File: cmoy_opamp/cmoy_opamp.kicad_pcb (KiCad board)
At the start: 2 copper layers, 79.2 x 67.6 mm, 33 parts, among them J1 AudioJack3, J2 AudioJack3, SW1 SPST, U1 MC33178, U2 LMH6642, U3 LMH6642, U4 LMH6642

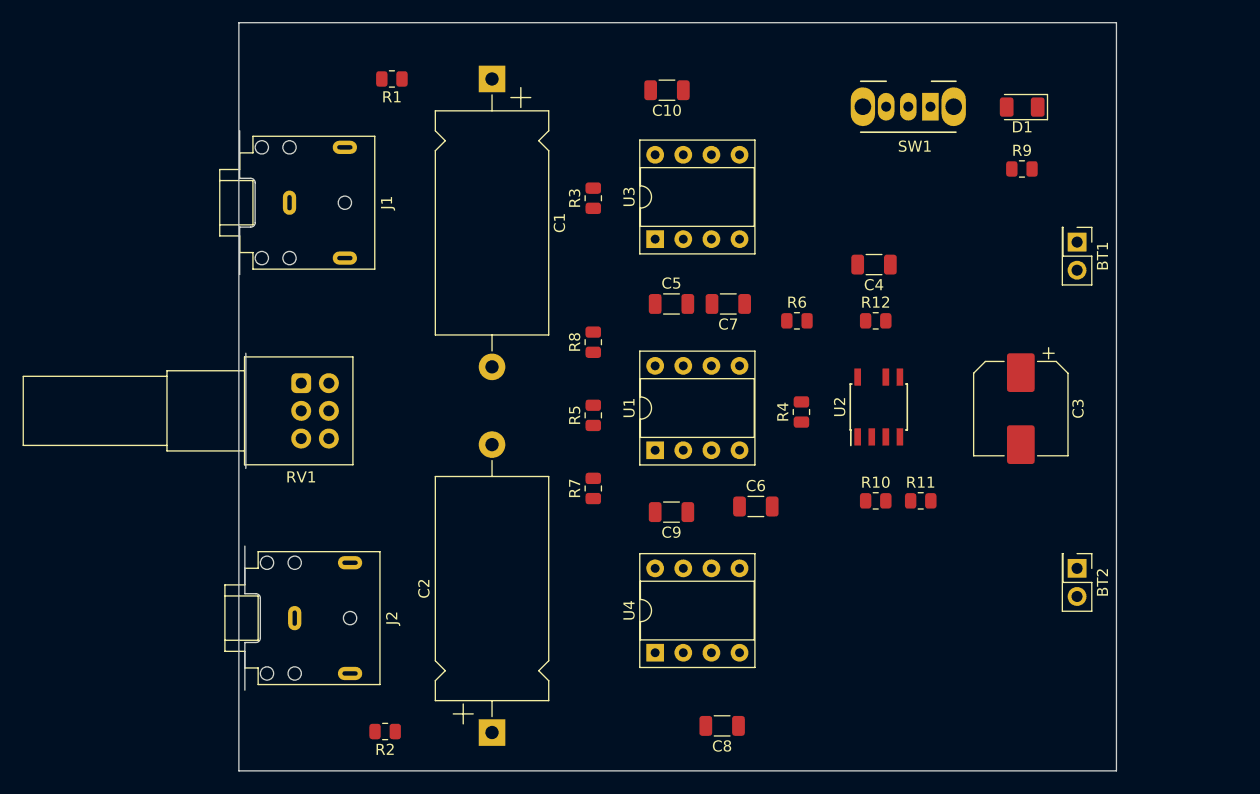
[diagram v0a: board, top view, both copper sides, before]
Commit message: dual footprint, THT and SMD, first layouting
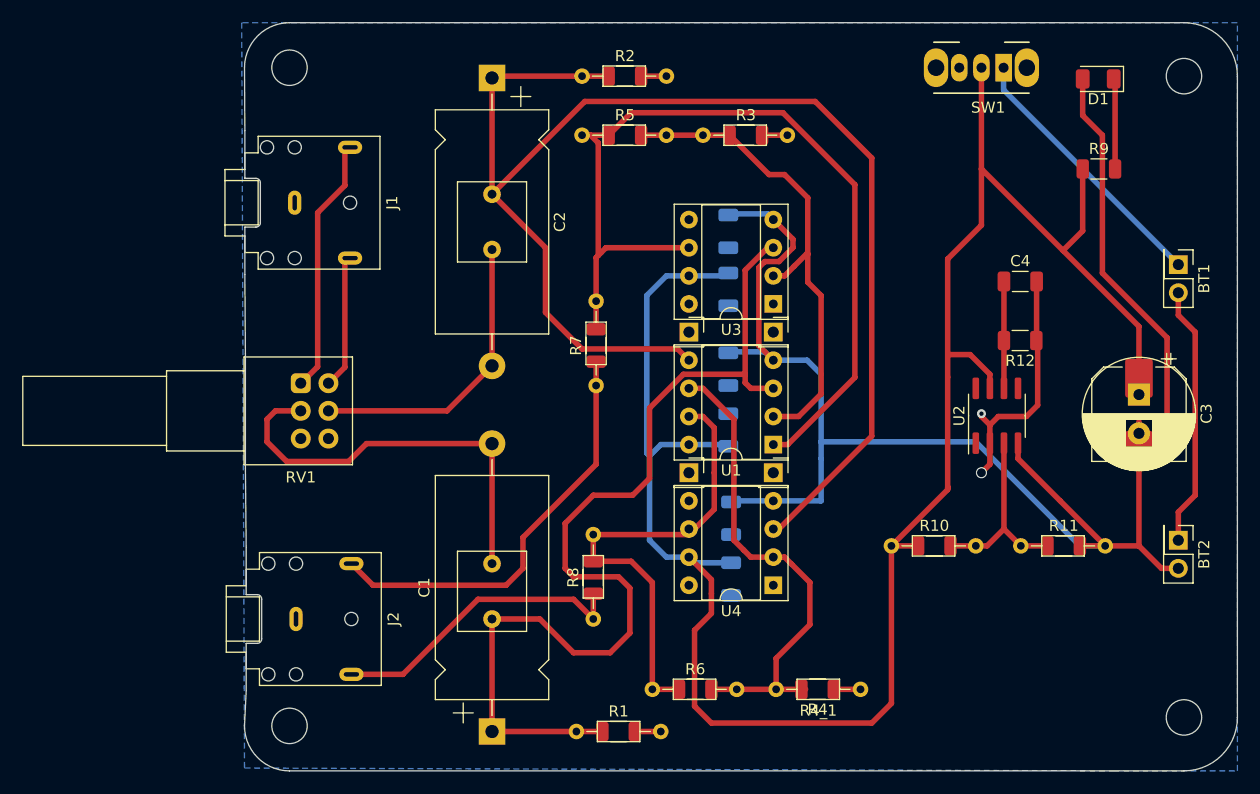
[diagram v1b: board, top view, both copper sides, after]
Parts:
- added C1_1: 0,1µF, Capacitor_THT:C_Rect_L7.0mm_W6.0mm_P5.00mm, F.Cu at (171.7, 92.0)
- added C2_1: 0,1µF, Capacitor_THT:C_Rect_L7.0mm_W6.0mm_P5.00mm, F.Cu at (171.7, 63.7)
- added C3_1: 220µF, Capacitor_THT:CP_Radial_D10.0mm_P3.50mm, F.Cu at (230.1, 76.8)
- added R10_1: 220k, Resistor_THT:R_Axial_DIN0204_L3.6mm_D1.6mm_P7.62mm_Horizontal, F.Cu at (207.8, 90.4)
- added R11_1: 220k, Resistor_THT:R_Axial_DIN0204_L3.6mm_D1.6mm_P7.62mm_Horizontal, F.Cu at (219.5, 90.4)
- added R1_1: 100k, Resistor_THT:R_Axial_DIN0204_L3.6mm_D1.6mm_P7.62mm_Horizontal, F.Cu at (179.3, 107.2)
- added R2_1: 100k, Resistor_THT:R_Axial_DIN0204_L3.6mm_D1.6mm_P7.62mm_Horizontal, F.Cu at (179.8, 48.0)
- added R3_1: 1k, Resistor_THT:R_Axial_DIN0204_L3.6mm_D1.6mm_P7.62mm_Horizontal, F.Cu at (190.8, 53.3)
- added R4_1: 1k, Resistor_THT:R_Axial_DIN0204_L3.6mm_D1.6mm_P7.62mm_Horizontal, F.Cu at (205.0, 103.4)
- added R5_1: 10k, Resistor_THT:R_Axial_DIN0204_L3.6mm_D1.6mm_P7.62mm_Horizontal, F.Cu at (179.8, 53.3)
- added R6_1: 10k, Resistor_THT:R_Axial_DIN0204_L3.6mm_D1.6mm_P7.62mm_Horizontal, F.Cu at (186.2, 103.4)
- added R7_1: 38, Resistor_THT:R_Axial_DIN0204_L3.6mm_D1.6mm_P7.62mm_Horizontal, F.Cu at (181.1, 75.9)
- added R8_1: 38, Resistor_THT:R_Axial_DIN0204_L3.6mm_D1.6mm_P7.62mm_Horizontal, F.Cu at (180.8, 97.0)
- added REF**: MountingHole_3.2mm_M3_ISO7380, MountingHole:MountingHole_3.2mm_M3_ISO7380, F.Cu at (153.4, 47.2)
- added REF**: MountingHole_3.2mm_M3_ISO7380, MountingHole:MountingHole_3.2mm_M3_ISO7380, F.Cu at (234.2, 105.9)
- added REF**: MountingHole_3.2mm_M3_ISO7380, MountingHole:MountingHole_3.2mm_M3_ISO7380, F.Cu at (234.2, 48.0)
- added REF**: MountingHole_3.2mm_M3_ISO7380, MountingHole:MountingHole_3.2mm_M3_ISO7380, F.Cu at (153.4, 106.7)
- added TP1: TestPoint, Connector_PinSocket_2.54mm:PinSocket_1x01_P2.54mm_Vertical, F.Cu at (189.5, 71.1)
- added TP2: TestPoint, Connector_PinSocket_2.54mm:PinSocket_1x01_P2.54mm_Vertical, F.Cu at (197.1, 71.1)
- added TP3: TestPoint, Connector_PinSocket_2.54mm:PinSocket_1x01_P2.54mm_Vertical, F.Cu at (189.5, 83.8)
- added TP4: TestPoint, Connector_PinSocket_2.54mm:PinSocket_1x01_P2.54mm_Vertical, F.Cu at (197.1, 83.8)
- C10, C5, C6, C7, C8, C9: moved to B.Cu
- R1, R10, R11, R12, R2, R3, R4, R5, R6, R7, R8, R9: footprint Resistor_SMD:R_0805_2012Metric -> Resistor_SMD:R_1206_3216Metric
- U2: footprint Package_SO:SOIC-8-N7_3.9x4.9mm_P1.27mm -> Package_SO:SOIC-8_3.9x4.9mm_P1.27mm
- moved R2 63.0 mm to (183.7, 48.0), turned to 0 degrees
- moved R1 62.4 mm to (183.1, 107.2), turned to 0 degrees
- moved C2 59.1 mm to (171.7, 48.2), turned to -90 degrees
- moved C1 58.9 mm to (171.7, 107.2), turned to 90 degrees
- moved R6 34.5 mm to (190.1, 103.4)
- moved R5 25.5 mm to (183.7, 53.3), turned to 0 degrees
- moved R4 25.1 mm to (201.1, 103.4), turned to 180 degrees
- moved R8 21.2 mm to (180.8, 93.3)
- moved C10 18.8 mm to (193.0, 67.3), turned to -90 degrees
- moved C8 18.8 mm to (193.3, 87.9), turned to -90 degrees
- moved R3 14.9 mm to (194.6, 53.3), turned to 0 degrees
- moved R11 13.5 mm to (223.3, 90.4)
- moved C4 13.3 mm to (219.4, 66.5), turned to 0 degrees
- moved R12 13.2 mm to (219.4, 71.9), turned to 180 degrees
- moved R7 12.9 mm to (181.1, 72.3)
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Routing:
- net V+: track 0.00 -> 182.3 mm
- net V-: track 0.00 -> 150.0 mm
- net /2+: track 0.00 -> 126.1 mm
- net /1+: track 0.00 -> 91.3 mm
- net /1O: track 0.00 -> 81.8 mm
- net /1-: track 0.00 -> 44.7 mm
- net /2-: track 0.00 -> 44.0 mm
- net /2O: track 0.00 -> 42.5 mm
- net Net-(J2-PadR): track 0.00 -> 38.3 mm
- net Net-(C1-Pad2): track 0.00 -> 38.0 mm
- net GND: track 0.00 -> 31.3 mm, vias 0 -> 2
- net Net-(J2-PadT): track 0.00 -> 27.7 mm
- net Net-(C2-Pad2): track 0.00 -> 26.9 mm
- net Net-(BT1-+): track 0.00 -> 24.3 mm
- net Net-(BT1--): track 0.00 -> 23.6 mm
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- added copper zone on B.Cu, net GND
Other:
- board size 79.2 x 67.6 mm -> 89.7 x 67.6 mm

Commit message: PCB Layout complete
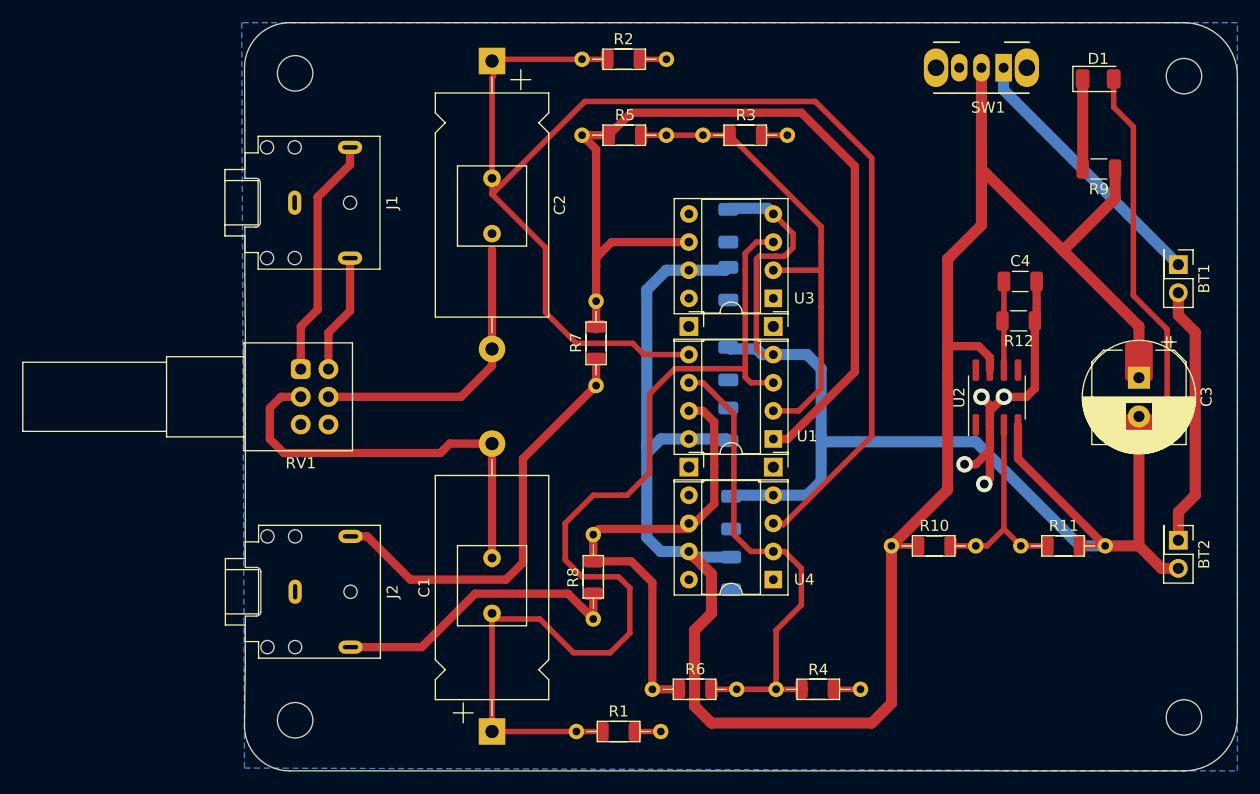
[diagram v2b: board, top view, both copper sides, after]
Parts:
- R9: value 100k -> 2k2
- moved J2 2.46 mm to (153.9, 94.6)
- moved R12 1.78 mm to (219.3, 70.1)
- moved U2 1.65 mm to (217.3, 77.0)
- moved R2 1.53 mm to (183.6, 46.5)
- moved C2 1.52 mm to (171.7, 46.6)
- moved C3 1.52 mm to (230.1, 77.0)
- moved C3_1 1.52 mm to (230.1, 75.2)
- moved R2_1 1.52 mm to (179.8, 46.5)
- moved C2_1 1.44 mm to (171.7, 62.2)
- moved RV1 1.27 mm to (154.4, 74.5)
- moved REF** 0.72 mm to (153.9, 106.2)
- moved REF** 0.72 mm to (153.9, 47.8)
- moved C1_1 0.51 mm to (171.7, 91.5)
- moved C6 0.51 mm to (193.0, 74.0)
- moved C8 0.51 mm to (193.3, 87.4)
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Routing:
- net GND: track 31.3 -> 36.1 mm, vias 2 -> 4
- net V+: track 182.3 -> 184.5 mm
- net /1O: track 81.8 -> 83.8 mm
- net Net-(C4-Pad1): track 9.65 -> 8.00 mm
- net Net-(U2-+): track 17.8 -> 19.4 mm
- net Net-(J1-PadT): track 11.9 -> 10.8 mm
- net Net-(J1-PadR): track 22.9 -> 21.9 mm
- net /1-: track 44.7 -> 43.8 mm
- net V-: track 150.0 -> 151.0 mm
- net /1+: track 91.3 -> 91.9 mm
- net Net-(J2-PadT): track 27.7 -> 27.1 mm
- net /2+: track 126.1 -> 125.6 mm
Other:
- outline, holes or cut-outs redrawn

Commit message: PCB art added
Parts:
- added G***: LOGO, pcb_art, F.Cu at (193.0, 78.2)
- added R12_1: 1k, Resistor_THT:R_Axial_DIN0204_L3.6mm_D1.6mm_P7.62mm_Horizontal, F.Cu at (223.0, 70.1)
- added REF**: OSHW-Logo2_14.6x12mm_Copper, Symbol:OSHW-Logo2_14.6x12mm_Copper, B.Cu at (222.8, 99.6)
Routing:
- net Net-(C4-Pad1): track 8.00 -> 10.4 mm
- net GND: track 36.1 -> 38.3 mm
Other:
- board text added: "www.designer2k2.at 2023"

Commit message: PCB Version ready to order
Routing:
- net Net-(C2-Pad2): track 26.4 -> 27.9 mm
- net /2+: track 125.6 -> 126.3 mm
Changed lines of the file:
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@@
   (segment (start 182.241 46.482) (end 179.832 46.482) (width 0.5) (layer "F.Cu") (net 6))
   (segment (start 180.08 50.292) (end 200.887949 50.292) (width 0.5) (layer "F.Cu") (net 6))
-  (segment (start 171.866 48.006) (end 171.704 48.168) (width 0.5) (layer "F.Cu") (net 6))
+  (segment (start 178.562 50.292) (end 180.08 50.292) (width 0.5) (layer "F.Cu") (net 6))
+  (segment (start 171.704 57.23) (end 177.88 51.054) (width 0.5) (layer "F.Cu") (net 6))
   (segment (start 197.104 88.392) (end 197.866 88.392) (width 0.5) (layer "F.Cu") (net 6))
+  (segment (start 177.88 51.054) (end 177.88 50.974) (width 0.5) (layer "F.Cu") (net 6))
   (segment (start 189.484 73.152) (end 185.42 73.152) (width 0.5) (layer "F.Cu") (net 6))
   (segment (start 179.751 46.482) (end 171.785 46.482) (width 0.5) (layer "F.Cu") (net 6))
   (segment (start 205.994 80.518) (end 197.993 88.519) (width 0.5) (layer "F.Cu") (net 6))
   (segment (start 200.887949 50.292) (end 205.994 55.398051) (width 0.5) (layer "F.Cu") (net 6))
-  (segment (start 176.53 63.494) (end 176.53 69.342) (width 0.5) (layer "F.Cu") (net 6))
   (segment (start 176.53 69.342) (end 179.324 72.136) (width 0.5) (layer "F.Cu") (net 6))
+  (segment (start 176.53 62.056) (end 176.53 63.754) (width 0.5) (layer "F.Cu") (net 6))
   (segment (start 197.866 88.392) (end 197.993 88.519) (width 0.5) (layer "F.Cu") (net 6))
-  (segment (start 171.704 48.168) (end 171.704 58.668) (width 0.5) (layer "F.Cu") (net 6))
   (segment (start 179.324 72.136) (end 184.404 72.136) (width 0.5) (layer "F.Cu") (net 6))
   (segment (start 205.994 55.398051) (end 205.994 80.518) (width 0.5) (layer "F.Cu") (net 6))
-  (segment (start 171.704 58.668) (end 176.53 63.494) (width 0.5) (layer "F.Cu") (net 6))
-  (segment (start 171.704 58.668) (end 180.08 50.292) (width 0.5) (layer "F.Cu") (net 6))
+  (segment (start 171.704 57.23) (end 171.704 46.644) (width 0.5) (layer "F.Cu") (net 6))
+  (segment (start 171.704 57.23) (end 176.53 62.056) (width 0.5) (layer "F.Cu") (net 6))
+  (segment (start 176.53 63.754) (end 176.53 69.342) (width 0.5) (layer "F.Cu") (net 6))
+  (segment (start 177.88 50.974) (end 178.562 50.292) (width 0.5) (layer "F.Cu") (net 6))
   (segment (start 185.42 73.152) (end 184.404 72.136) (width 0.5) (layer "F.Cu") (net 6))
+  (segment (start 156.932 76.962) (end 168.91 76.962) (width 0.75) (layer "F.Cu") (net 7))
   (segment (start 168.91 76.962) (end 171.704 74.168) (width 0.75) (layer "F.Cu") (net 7))
-  (segment (start 156.932 76.962) (end 168.91 76.962) (width 0.75) (layer "F.Cu") (net 7))
-  (segment (start 171.704 63.668) (end 171.704 74.168) (width 0.75) (layer "F.Cu") (net 7))
+  (segment (start 171.704 74.168) (end 171.704 62.23) (width 0.75) (layer "F.Cu") (net 7))
   (segment (start 191.516 92.964) (end 191.516 96.52) (width 1) (layer "F.Cu") (net 8))
   (segment (start 212.852 72.39) (end 212.852 64.516) (width 1) (layer "F.Cu") (net 8))

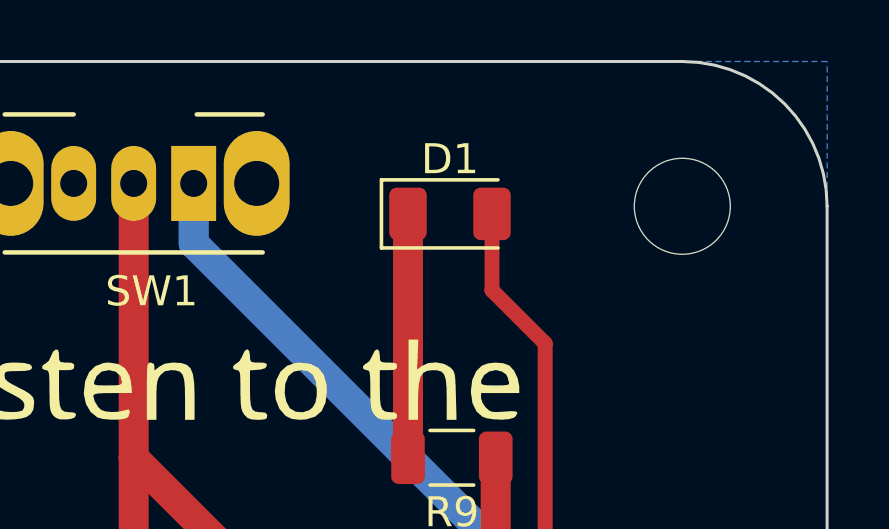
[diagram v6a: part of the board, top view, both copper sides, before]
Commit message: fully remove rescue lib reference
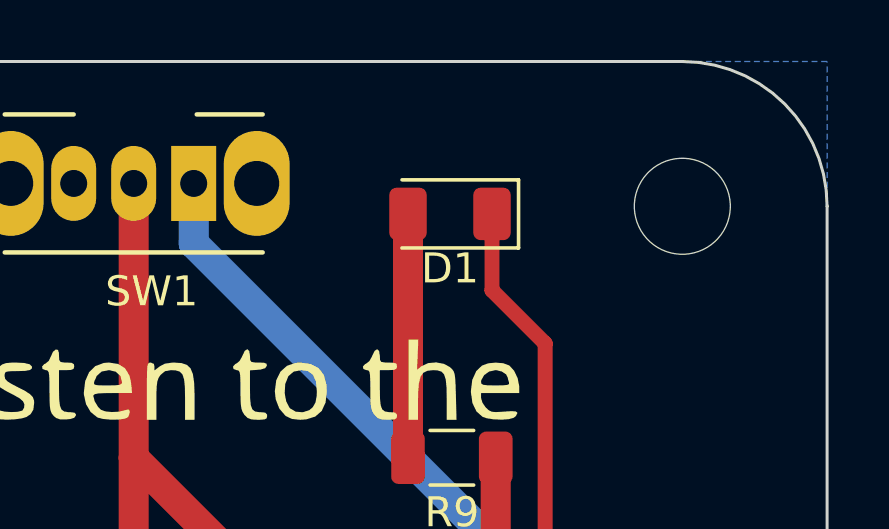
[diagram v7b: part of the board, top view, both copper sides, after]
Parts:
- turned D1 to 180 degrees
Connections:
- D1 pad 1: Net-(D1-A) -> V-
- D1 pad 2: V- -> Net-(D1-A)
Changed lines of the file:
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@@
   )
   (footprint "LED_SMD:LED_1206_3216Metric" (layer "F.Cu")
-    (at 226.444 48.26)
+    (at 226.444 48.26 180)
     (descr "LED SMD 1206 (3216 Metric), square (rectangular) end terminal, IPC_7351 nominal, (Body size source: http://www.tortai-tech.com/upload/download/2011102023233369053.pdf), generated with kicad-footprint-generator")
     (tags "LED")
     (property "Sheetfile" "cmoy_opamp.kicad_sch")
     (property "Sheetname" "")
+    (property "ki_description" "Light emitting diode")
+    (property "ki_keywords" "LED diode")
     (attr smd)
     (fp_text reference "D1" (at 0 -1.82) (layer "F.SilkS")
@@
     (fp_line (start 1.6 0.8) (end 1.6 -0.8)
       (stroke (width 0.1) (type solid)) (layer "F.Fab"))
-    (pad "1" smd roundrect (at -1.4 0) (size 1.25 1.75) (layers "F.Cu" "F.Paste" "F.Mask") (roundrect_rratio 0.2)
-      (net 11 "Net-(D1-A)") (pinfunction "A") (pintype "passive"))
-    (pad "2" smd roundrect (at 1.4 0) (size 1.25 1.75) (layers "F.Cu" "F.Paste" "F.Mask") (roundrect_rratio 0.2)
+    (pad "1" smd roundrect (at -1.4 0 180) (size 1.25 1.75) (layers "F.Cu" "F.Paste" "F.Mask") (roundrect_rratio 0.2)
       (net 3 "V-") (pinfunction "K") (pintype "passive"))
+    (pad "2" smd roundrect (at 1.4 0 180) (size 1.25 1.75) (layers "F.Cu" "F.Paste" "F.Mask") (roundrect_rratio 0.2)
+      (net 11 "Net-(D1-A)") (pinfunction "A") (pintype "passive"))
     (model "${KICAD6_3DMODEL_DIR}/LED_SMD.3dshapes/LED_1206_3216Metric.wrl"
       (offset (xyz 0 0 0))
@@
     (property "Sheetfile" "cmoy_opamp.kicad_sch")
     (property "Sheetname" "")
+    (property "ki_description" "Dual Low Power, Low Noise Operational Amplifiers, DIP-8/SOIC-8/SSOP-8")
+    (property "ki_keywords" "dual opamp")
     (attr through_hole)
     (fp_text reference "U1" (at -3.048 0.254) (layer "F.SilkS")
@@
     (property "Sheetfile" "cmoy_opamp.kicad_sch")
     (property "Sheetname" "")
+    (property "ki_description" "Single Pole Single Throw (SPST) switch")
+    (property "ki_keywords" "switch lever")
     (attr through_hole)
     (fp_text reference "SW1" (at 1.4 -3.6) (layer "F.SilkS")
@@
     (pad "" thru_hole oval (at 6.1 0 180) (size 2.2 3.5) (drill 1.5) (layers "*.Cu" "*.Mask"))
     (pad "1" thru_hole rect (at 0 0 180) (size 1.5 2.5) (drill 0.9) (layers "*.Cu" "*.Mask")
-      (net 1 "Net-(BT1-+)") (pinfunction "1") (pintype "input"))
+      (net 1 "Net-(BT1-+)") (pinfunction "A") (pintype "passive"))
     (pad "2" thru_hole oval (at 2 0 180) (size 1.5 2.5) (drill 0.9) (layers "*.Cu" "*.Mask")
-      (net 8 "V+") (pinfunction "2") (pintype "input"))
+      (net 8 "V+") (pinfunction "B") (pintype "passive"))
     (pad "3" thru_hole oval (at 4 0 180) (size 1.5 2.5) (drill 0.9) (layers "*.Cu" "*.Mask"))
     (model "${KICAD6_3DMODEL_DIR}/Button_Switch_THT.3dshapes/SW_CuK_OS102011MA1QN1_SPDT_Angled.wrl"
@@
     (property "Sheetfile" "cmoy_opamp.kicad_sch")
     (property "Sheetname" "")
+    (property "ki_description" "Dual potentiometer")
+    (property "ki_keywords" "resistor variable")
     (attr through_hole)
     (fp_text reference "RV1" (at 0 8.5 180) (layer "F.SilkS")
@@
       (net 10 "GND") (pinfunction "3") (pintype "passive"))
     (pad "4" thru_hole circle (at 2.5 0 180) (size 1.8 1.8) (drill 1) (layers "*.Cu" "*.Mask")
-      (net 13 "Net-(J1-PadT)") (pintype "passive"))
+      (net 13 "Net-(J1-PadT)") (pinfunction "4") (pintype "passive"))
     (pad "5" thru_hole circle (at 2.5 2.5 180) (size 1.8 1.8) (drill 1) (layers "*.Cu" "*.Mask")
-      (net 7 "Net-(C2-Pad2)") (pintype "passive"))
+      (net 7 "Net-(C2-Pad2)") (pinfunction "5") (pintype "passive"))
     (pad "6" thru_hole circle (at 2.5 5 180) (size 1.8 1.8) (drill 1) (layers "*.Cu" "*.Mask")
-      (net 10 "GND") (pintype "passive"))
+      (net 10 "GND") (pinfunction "6") (pintype "passive"))
     (model "${KICAD6_3DMODEL_DIR}/Potentiometer_THT.3dshapes/Potentiometer_Alps_RK097_Dual_Horizontal.wrl"
       (offset (xyz 0 0 0))
@@
   (segment (start 229.616 52.578) (end 227.844 50.806) (width 0.5) (layer "F.Cu") (net 3))
   (segment (start 230.124 90.424) (end 230.124 81.788) (width 1) (layer "F.Cu") (net 3))
-  (segment (start 227.844 50.806) (end 227.844 48.26) (width 0.5) (layer "F.Cu") (net 3))
   (segment (start 232.664 70.866) (end 229.616 67.818) (width 0.5) (layer "F.Cu") (net 3))
   (segment (start 219.202 79.502) (end 219.202 82.55) (width 0.75) (layer "F.Cu") (net 3))
@@
   (segment (start 197.104 73.152) (end 196.088 73.152) (width 0.5) (layer "F.Cu") (net 3))
   (segment (start 229.616 67.818) (end 229.616 52.578) (width 0.5) (layer "F.Cu") (net 3))
+  (segment (start 227.844 48.26) (end 227.844 50.806) (width 0.5) (layer "F.Cu") (net 3))
   (segment (start 198.882 63.5) (end 198.1 64.282) (width 0.5) (layer "F.Cu") (net 3))
   (segment (start 232.664 79.248) (end 232.664 70.866) (width 0.5) (layer "F.Cu") (net 3))
